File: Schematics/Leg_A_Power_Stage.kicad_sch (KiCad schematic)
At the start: 0 parts

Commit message: [LEG A WIP]
- moved circuits in Leg A HS and LS
- Completed 90% of HS and LS for LEG A
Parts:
- added C17, C22: 15 u, symbol Device:C
- added C18, C19, C21, C24, C26, C29: 0.1 u, symbol Device:C
- added C20, C23, C27, C30: 1 u, symbol Device:C
- added D3, D4: BZX84C20-7-F, Package_TO_SOT_SMD:SOT-23-3, symbol SiC_Inverter:BZX84C20-7-F
- added Q3, Q7: C3M0025065K, SiC_Inverter:C3M0025065K, symbol SiC_Inverter:C3M0025065K
- added R10, R12, R16, R17, R18, R19: 10K, Resistor_SMD:R_1206_3216Metric_Pad1.30x1.75mm_HandSolder, symbol Device:R
- added R11, R9: 100, Resistor_SMD:R_1206_3216Metric_Pad1.30x1.75mm_HandSolder, symbol Device:R
- added R13, R8: 100K, Resistor_SMD:R_1206_3216Metric_Pad1.30x1.75mm_HandSolder, symbol Device:R
- added R14, R15, R6, R7: 10, Resistor_SMD:R_1206_3216Metric_Pad1.30x1.75mm_HandSolder, symbol Device:R
- added U1, U2: UCC21710QDWRQ1, SiC_Inverter:UCC21710QDWRQ1, symbol SiC_Inverter:UCC21710QDWRQ1
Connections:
- new net: C24.1, R11.1, U2.10 (IN+)
- new net: C21.1, R9.1, U1.10 (IN+)
- new net +15V_ISO_LALS: C17.1, C29.1, C30.1, U2.5 (VDD)
- new net +15V__ISO_LAHS: C22.1, C26.1, C27.1, U1.5 (VDD)
- new net +3V3: C18.1, C19.1, C20.1, C23.1, R10.1, R12.1, R16.1, R17.1, R18.1, R19.1, U1.15 (VCC), U2.15 (VCC)
- new net BUS_DC+: Q3.1
- new net GND_ISO_LAHS: C22.2, C26.2, C27.2, D3.2 (A), Q3.2, Q3.3, Q7.1, R13.2, U1.1 (AIN), U1.2 (OC), U1.3 (COM), U1.8 (VEE)
- new net GND_ISO_LALS: C17.2, C29.2, C30.2, D4.2 (A), Q7.2, Q7.3, R8.2, U2.1 (AIN), U2.2 (OC), U2.3 (COM), U2.8 (VEE)
- new net HS_LegA_EN: R12.2, U1.14 (~{RST}/EN)
- new net HS_LegA_RDY: R16.2, U1.12 (RDY)
- new net LOGIC_GND: C18.2, C19.2, C20.2, C21.2, C23.2, C24.2, U1.11 (IN-), U1.9 (GND), U2.11 (IN-), U2.9 (GND)
- new net LS_LegA_EN: R10.2, U2.14 (~{RST}/EN)
- new net LS_LegA_RDY: R19.2, U2.12 (RDY)
- new net LegA_HS_Gate: D3.1 (K), Q3.4, R13.1, R6.2, R7.2, U1.7 (CLMPI)
- new net LegA_HS_OUTH: R6.1, U1.4 (OUTH)
- new net LegA_HS_OUTL: R7.1, U1.6 (OUTL)
- new net LegA_LS_Gate: D4.1 (K), Q7.4, R14.2, R15.2, R8.1, U2.7 (CLMPI)
- new net LegA_LS_OUTH: R15.1, U2.4 (OUTH)
- new net LegA_LS_OUTL: R14.1, U2.6 (OUTL)
- new net PWM_A_H: R9.2
- new net PWM_A_L: R11.2
- new net ~{HS_LegA_FLT}: R17.2, U1.13 (~{FLT})
- new net ~{LS_LegA_FLT}: R18.2, U2.13 (~{FLT})
- no-connect marks 0 -> 2
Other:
- note added: "Ceramic"
- note added: "High Side"
- note added: "Leg A"
- note added: "Low Side"
- note added: "Need a Isoulated DC-DC Converter for this. THe 15V output will be +15V_ISO_LAHS and GND_ISO_LAHS"
- note added: "Need a Isoulated DC-DC Converter for this. THe 15V output will be +15V_ISO_LALS and GND_ISO_LALS"
- note added: "Pick out 15 uF, 0.1 uF , and 1 uF cap and fill out footprint Before moving on to the Low Side for Leg A"
- note added: "R0ff"
- note added: "Ron"

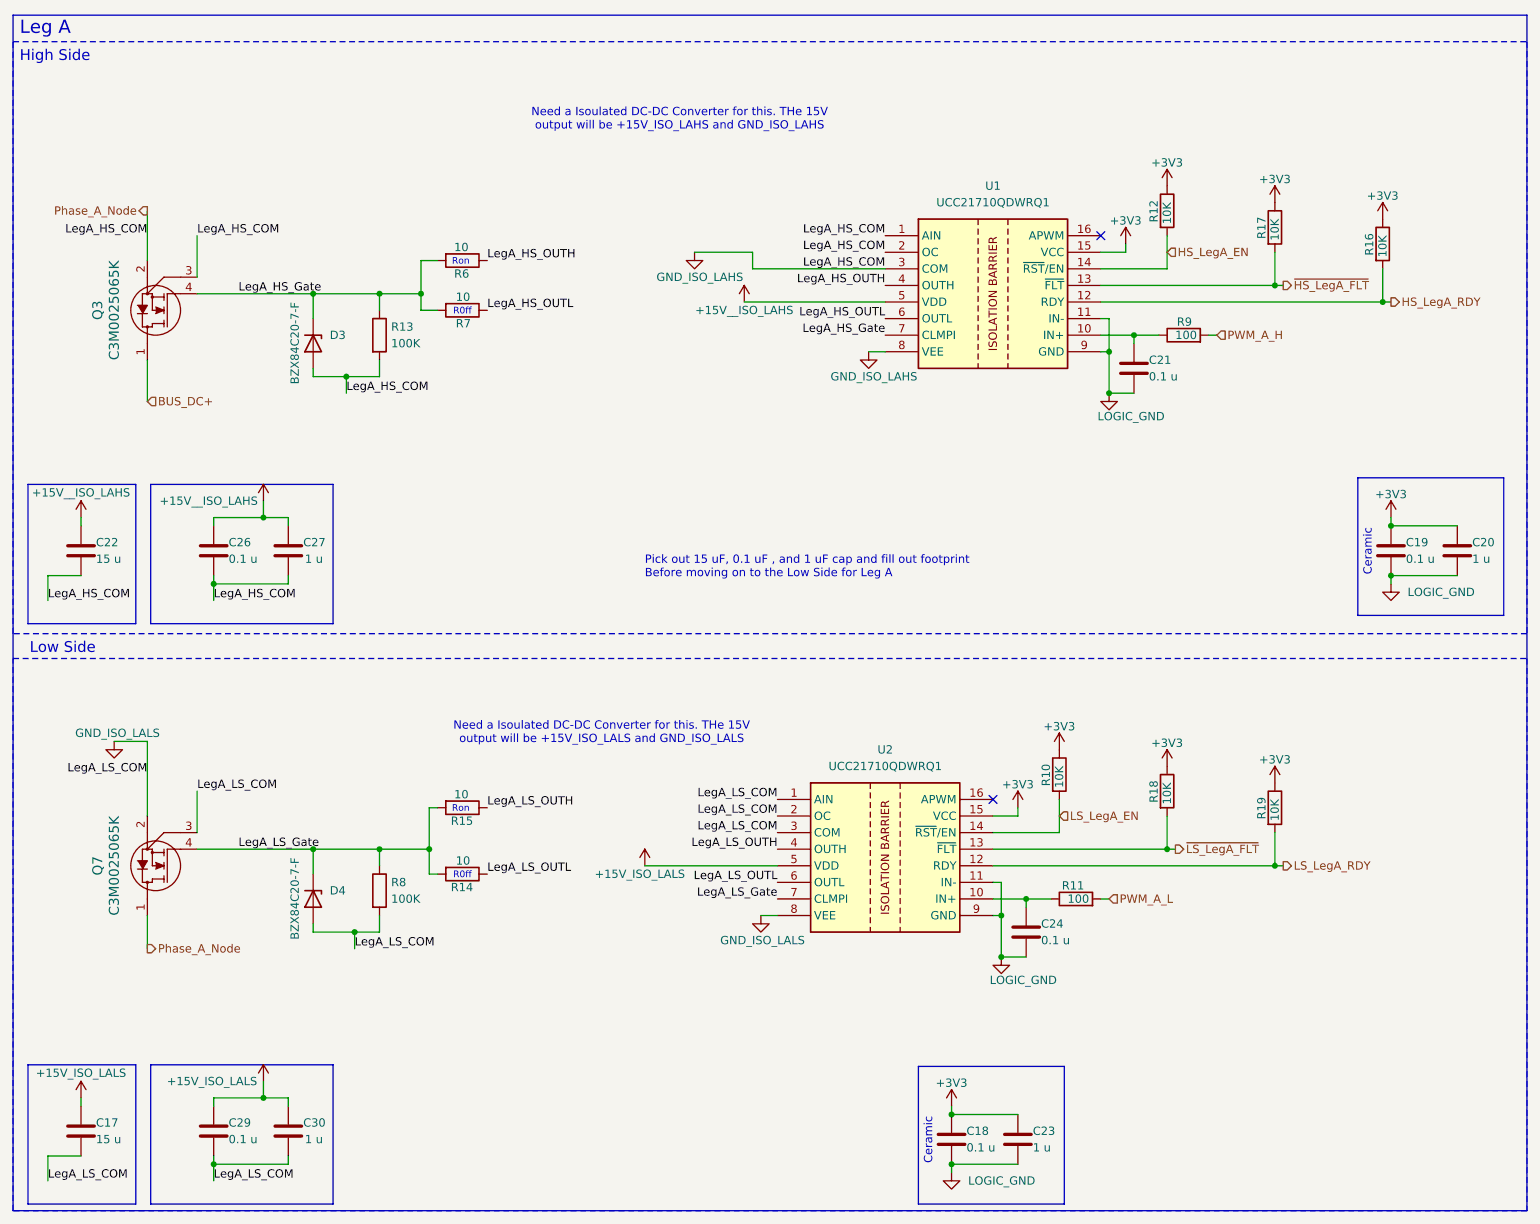
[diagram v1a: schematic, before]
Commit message: Adding 100 pf caps to Leg A circuit, WIP texts
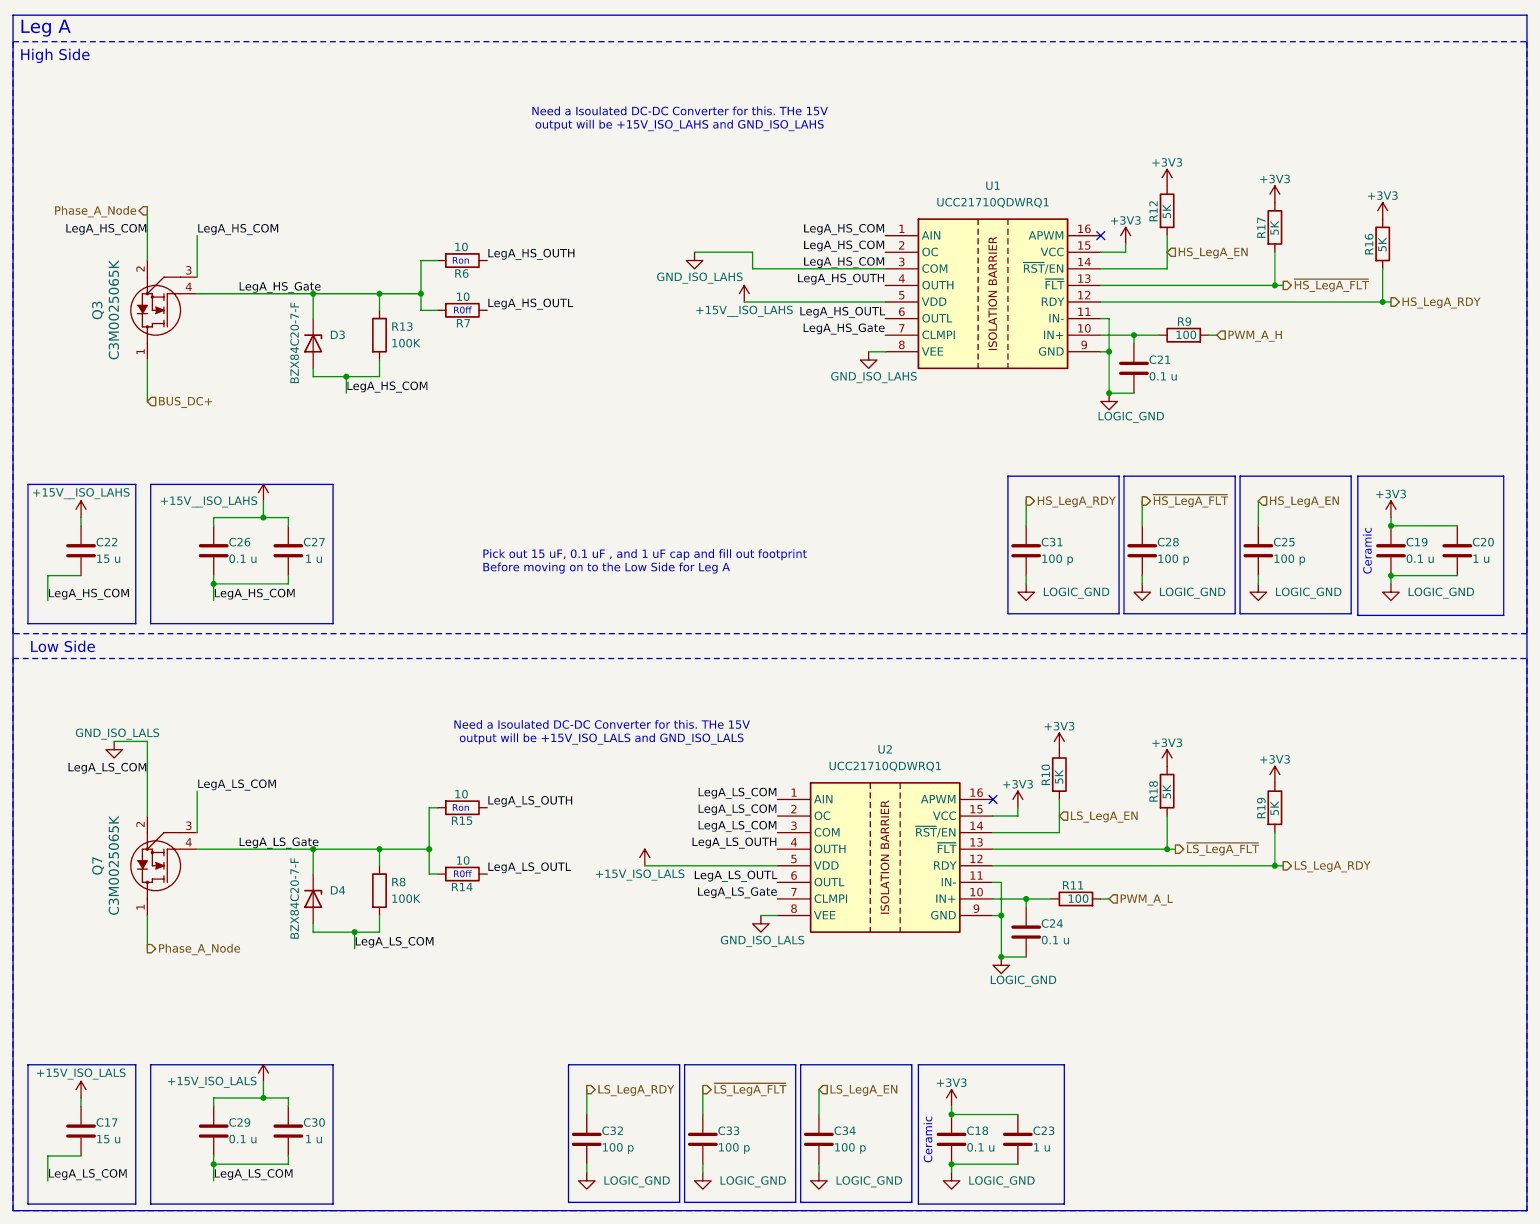
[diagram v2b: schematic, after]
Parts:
- added C25, C28, C31, C32, C33, C34: 100 p, symbol Device:C
- R10, R12, R16, R17, R18, R19: value 10K -> 5K
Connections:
- net HS_LegA_EN: now also C25.1
- net HS_LegA_RDY: now also C31.1
- net LOGIC_GND: now also C25.2, C28.2, C31.2, C32.2, C33.2, C34.2
- net LS_LegA_EN: now also C34.1
- net LS_LegA_RDY: now also C32.1
- net ~{HS_LegA_FLT}: now also C28.1
- net ~{LS_LegA_FLT}: now also C33.1

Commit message: Copy past Leg A onto Leg B, Changed hames on both High/Low side to match Leg B
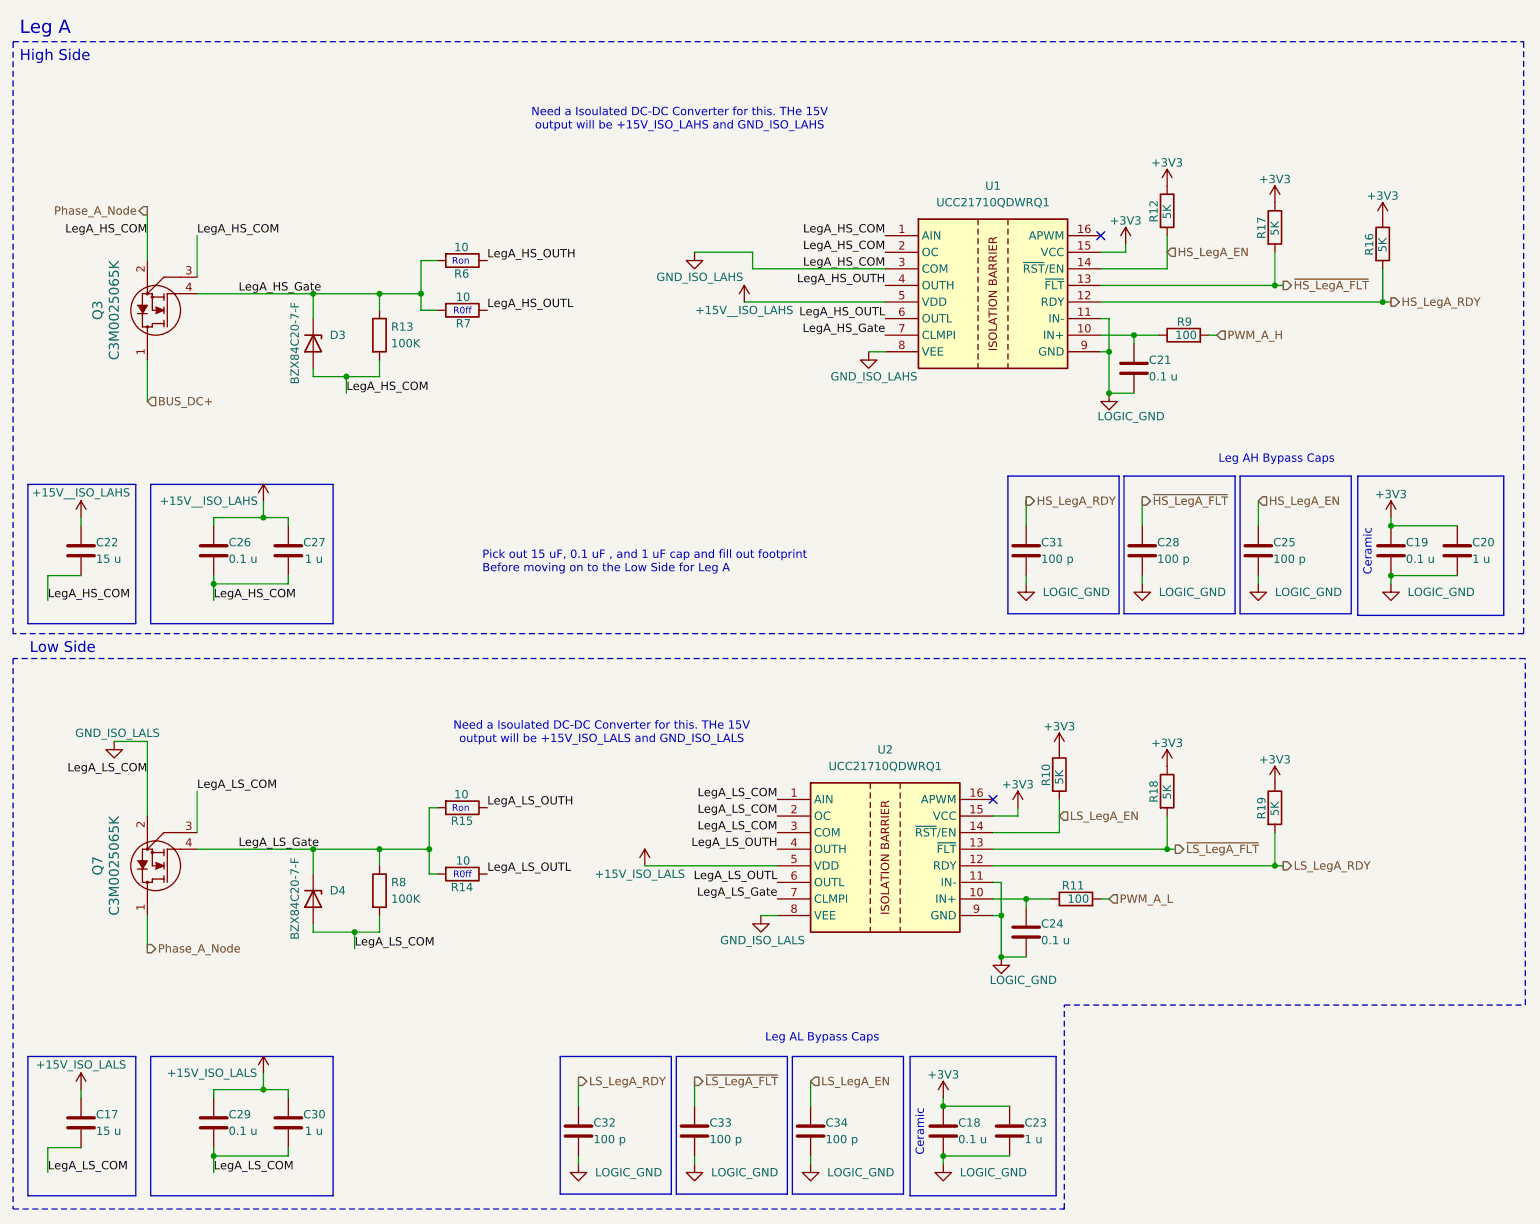
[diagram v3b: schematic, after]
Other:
- note added: "Leg AH Bypass Caps"
- note added: "Leg AL Bypass Caps"
- moved on the sheet: C17, C18, C23, C29, C30, C32, C33, C34

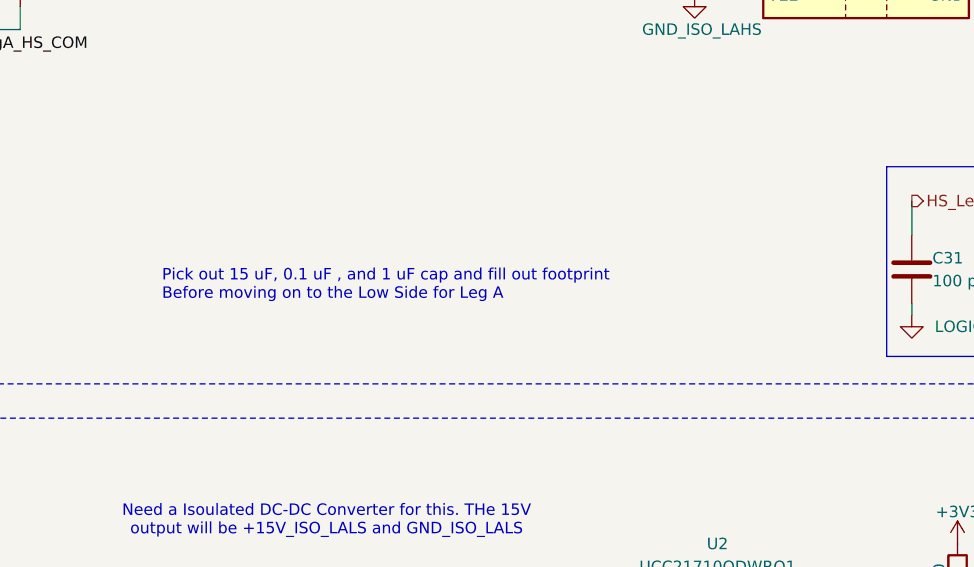
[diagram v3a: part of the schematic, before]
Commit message: Added Footprints for Cap size 15u, 1u, 0.1u and 100p
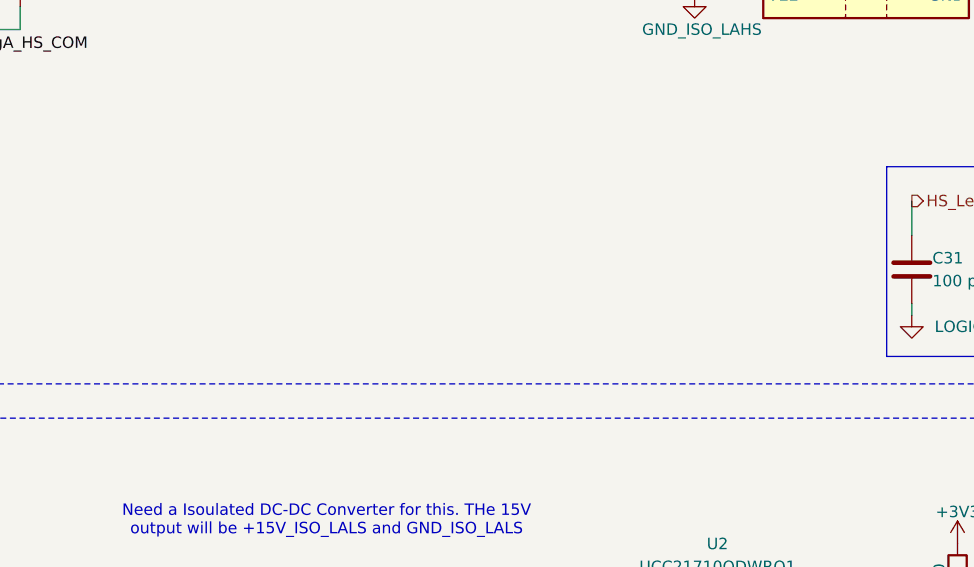
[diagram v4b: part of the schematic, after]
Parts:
- C17, C22: footprint (none) -> Capacitor_SMD:C_1206_3216Metric_Pad1.33x1.80mm_HandSolder; symbol Device:C -> SiC_Inverter:C3216X5R1E156M160AB
- C18, C19, C21, C24, C26, C29: footprint (none) -> Capacitor_SMD:C_0805_2012Metric_Pad1.18x1.45mm_HandSolder; symbol Device:C -> SiC_Inverter:C2012X8R1E105M125AE
- C20, C23, C27, C30: footprint (none) -> Capacitor_SMD:C_1206_3216Metric_Pad1.33x1.80mm_HandSolder; symbol Device:C -> SiC_Inverter:C3216X8R1E105M160AA
- C25, C28, C31, C32, C33, C34: footprint (none) -> Capacitor_SMD:C_0603_1608Metric_Pad1.08x0.95mm_HandSolder; symbol Device:C -> SiC_Inverter:CGA1A2X7R1C101K030BA
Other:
- note removed: "Pick out 15 uF, 0.1 uF , and 1 uF cap and fill out footprint Before moving on to the Low Side for Leg A"
